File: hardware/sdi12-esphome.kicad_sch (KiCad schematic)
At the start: 32 parts, among them J0 Grounding, J1 SDI-12 A, J2 SDI-12 B, J3 SDI-12 C, J4 SDI-12 D, J5 GPIO21/22, J6 Rain Gauge, Q1 2N7002, Q2 AO3401A, U1 ESP32_NODEMCU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

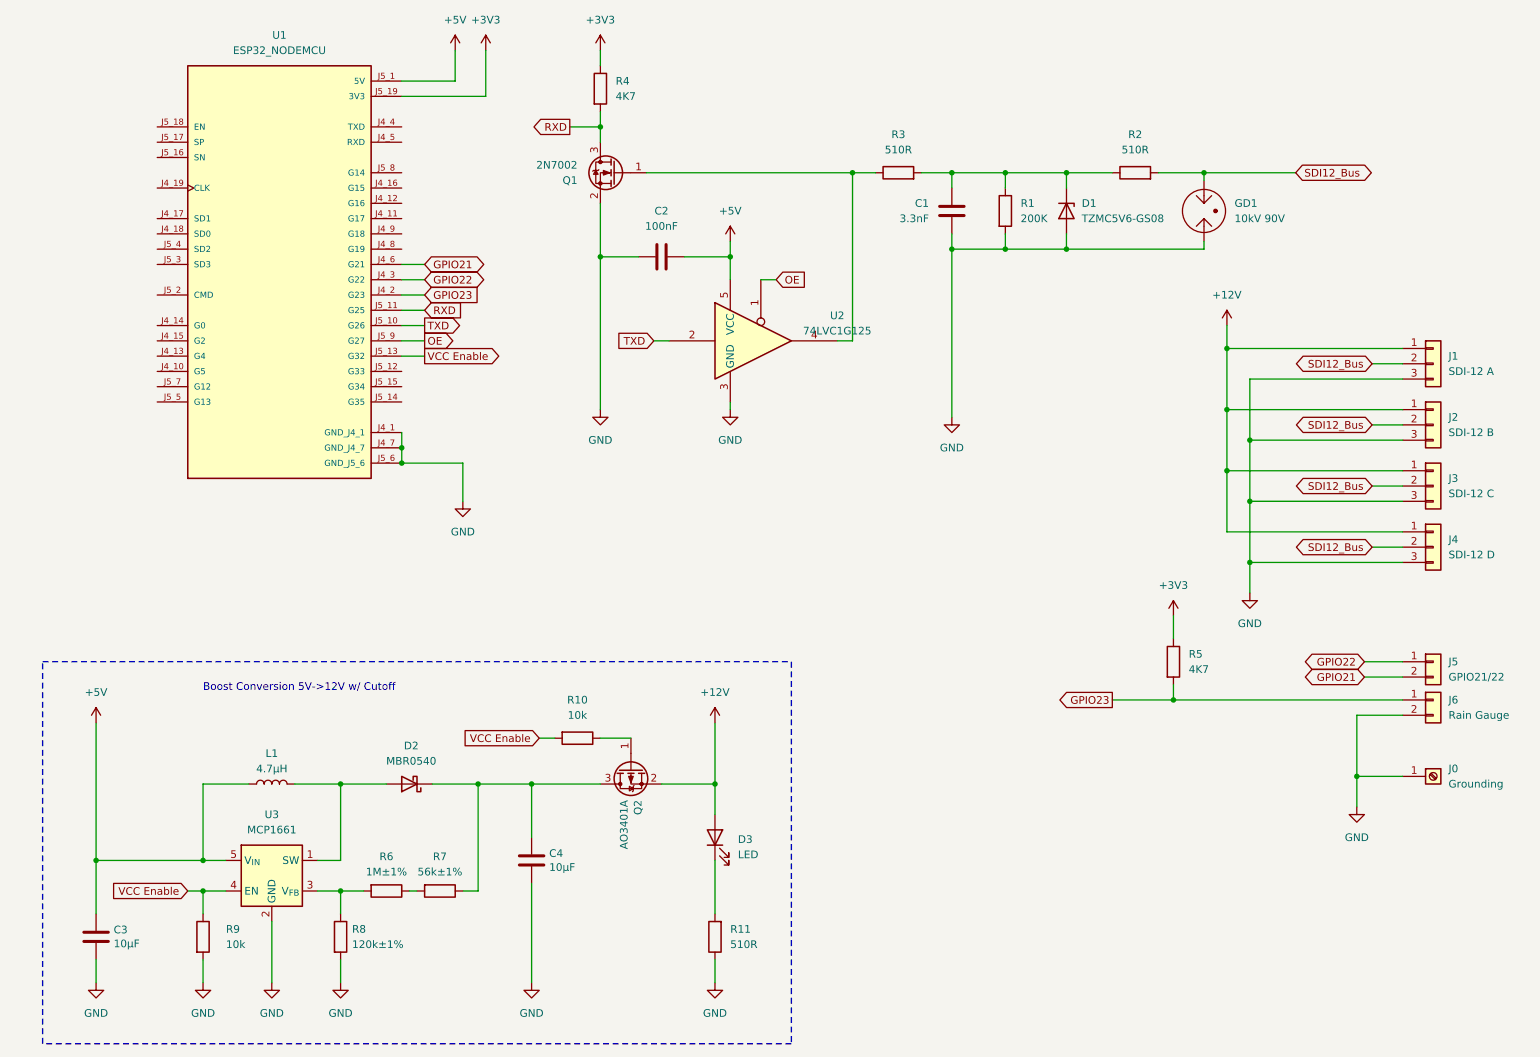
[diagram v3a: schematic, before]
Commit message: Schematic: Add additional NPN for level shifting the BusPwrEnable signal
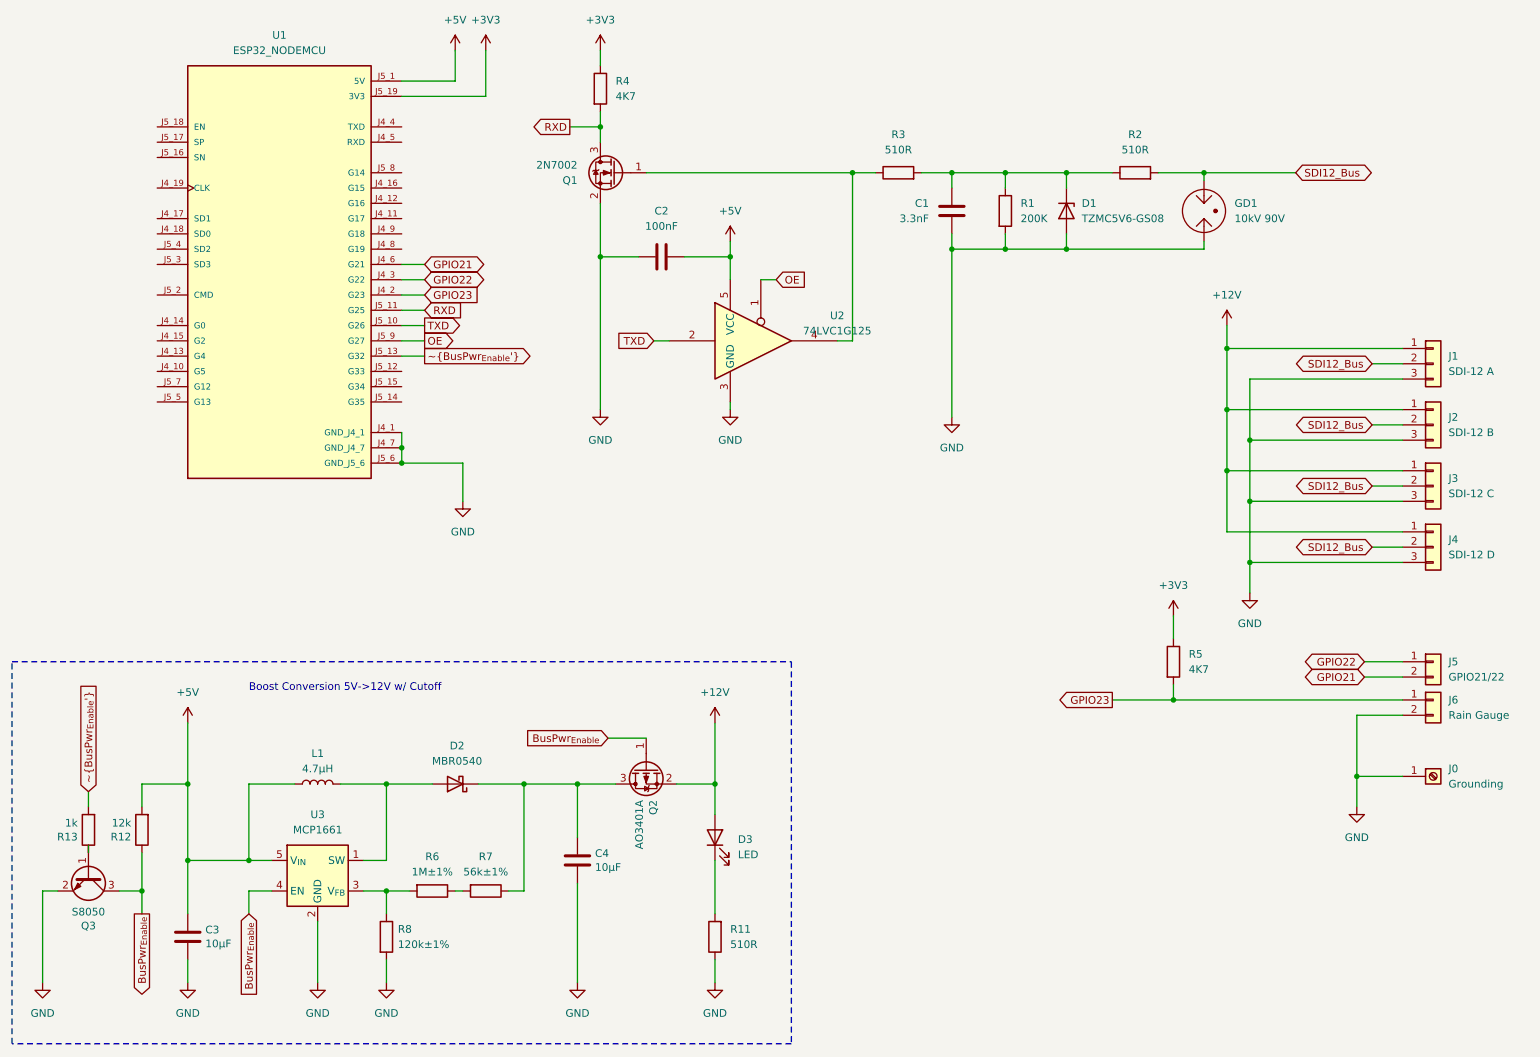
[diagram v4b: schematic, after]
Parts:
- removed R10, R9: 10k, Resistor_SMD:R_0805_2012Metric_Pad1.20x1.40mm_HandSolder, symbol Device:R
- added Q3: S8050, Package_TO_SOT_SMD:SOT-23, symbol fraxinas:S8050-SOT23
- added R12: 12k, Resistor_SMD:R_0805_2012Metric_Pad1.20x1.40mm_HandSolder, symbol Device:R
- added R13: 1k, Resistor_SMD:R_0805_2012Metric_Pad1.20x1.40mm_HandSolder, symbol Device:R
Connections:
- net +5V: now also R12.2
- net GND: now also Q3.2 (E)
- net BusPwr_{Enable}: now reaches Q2.1 (G)
- net BusPwr_{Enable}: now also U3.4 (EN), Q3.3 (C), R12.1
- net VCC Enable renamed ~{BusPwr_{Enable}'}
- net ~{BusPwr_{Enable}'}: now also R13.2; no longer U3.4 (EN)
- new net: Q3.1 (B), R13.1
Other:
- moved on the sheet: C3, C4, D2, L1, Q2, R6, R7, R8, U3

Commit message: Add Header for RCWL-1655 Distance Sensor Module
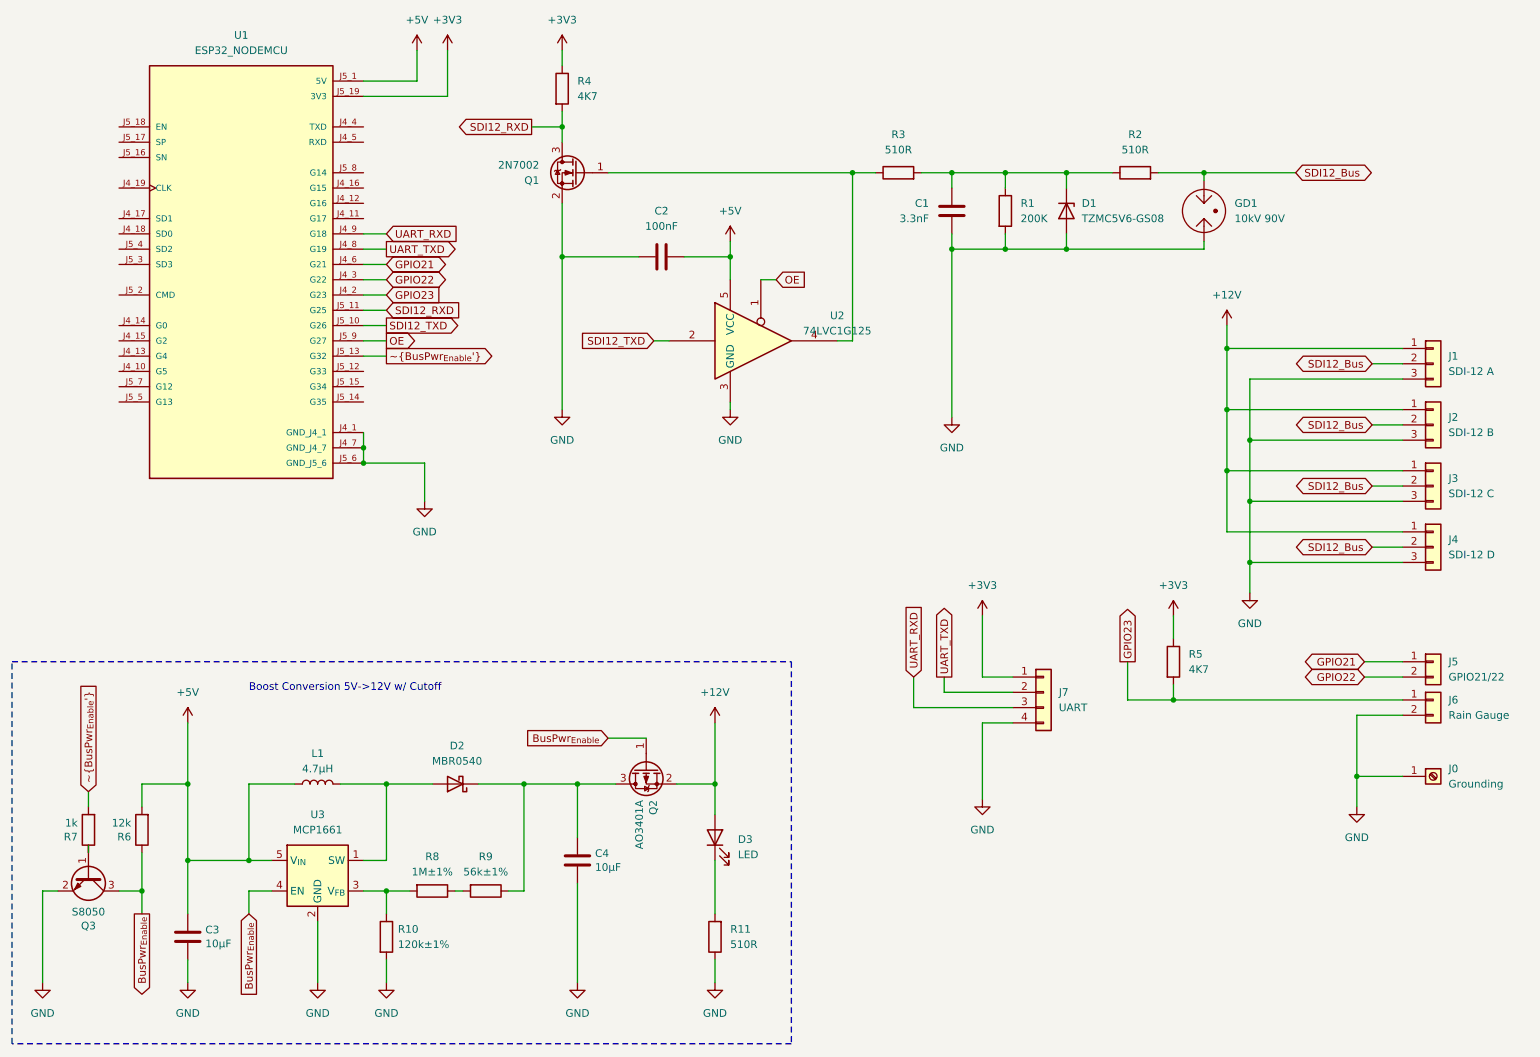
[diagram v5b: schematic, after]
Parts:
- added J7: UART, Connector_PinSocket_2.54mm:PinSocket_1x04_P2.54mm_Vertical, symbol Connector_Generic:Conn_01x04
- renumbered R8 to R10, R12 to R6, R13 to R7, R6 to R8, R7 to R9
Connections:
- net +3V3: now also J7.1 (Pin_1)
- net GND: now also J7.4 (Pin_4)
- net GPIO21: now also J5.1 (Pin_1); no longer J5.2 (Pin_2)
- net GPIO22: now also J5.2 (Pin_2); no longer J5.1 (Pin_1)
- net UART_TXD: now reaches U1.J4_8 (G19)
- net UART_TXD: now also J7.2 (Pin_2)
- net UART_RXD: now reaches U1.J4_9 (G18)
- net UART_RXD: now also J7.3 (Pin_3)
- net RXD renamed SDI12_RXD
- net TXD renamed SDI12_TXD
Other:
- moved on the sheet: Q1, R4, U1
